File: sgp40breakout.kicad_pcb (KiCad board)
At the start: 2 copper layers, 15 x 11.2 mm, 13 parts, among them J1 Conn_01x04_Male, U1 SGP40, U2 SHT35-DIS

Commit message: add missing file, fix back silk screen
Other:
- board text added: "SGP40 SHT35-DIS VOC Sensor v0.1"
- board text removed: "SGP40 SHT35-D VOC Sensor v0.1"

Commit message: remove most gold plating from mounting hole
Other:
- board text added: "Sensirion SGP40 SHT35-DIS"
- board text added: "v0.1"
- board text removed: "SGP40 SHT35-DIS VOC Sensor v0.1"
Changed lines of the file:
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@@
   (general
     (thickness 1.6002)
-    (drawings 13)
+    (drawings 14)
     (tracks 89)
     (zones 0)
@@
     (mod_text_size 1 1)
     (mod_text_width 0.15)
-    (pad_size 1.524 1.524)
-    (pad_drill 0.762)
+    (pad_size 2.4 2.4)
+    (pad_drill 2.2)
     (pad_to_mask_clearance 0.000051)
     (aux_axis_origin 0 0)
@@
       (effects (font (size 1 1) (thickness 0.15)))
     )
-    (pad 1 thru_hole circle (at 0 0) (size 4.4 4.4) (drill 2.2) (layers *.Cu *.Mask))
+    (pad 1 thru_hole circle (at 0 0) (size 2.4 2.4) (drill 2.2) (layers *.Cu *.Mask))
   )
   (module sgp40breakout:Sensirion_DFN-6-1EP_2.44x2.44mm_P0.8mm (layer F.Cu)
@@
       (net 2 "Net-(C1-Pad2)"))
   )
-  (gr_text "SGP40\nSHT35-DIS\nVOC Sensor\nv0.1" (at 130.302 80.01 270) (layer B.SilkS)
+  (gr_text v0.1 (at 135.636 82.042 270) (layer B.Cu)
+    (effects (font (size 0.8 0.8) (thickness 0.2)) (justify mirror))
+  )
+  (gr_text "Sensirion\nSGP40\nSHT35-DIS" (at 130.302 80.01 270) (layer B.SilkS)
     (effects (font (size 0.8 0.8) (thickness 0.15)) (justify mirror))
   )

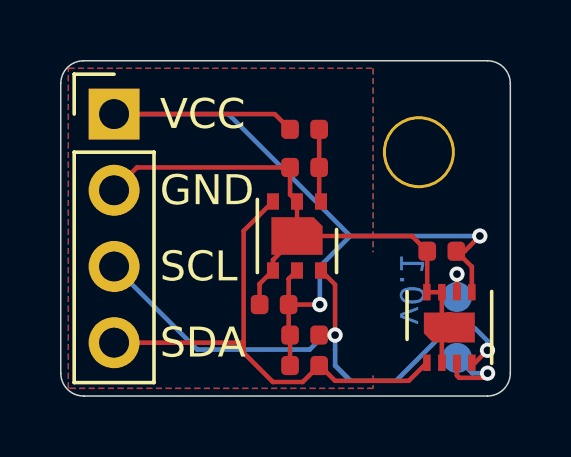
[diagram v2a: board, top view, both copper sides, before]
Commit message: add OSHW logo
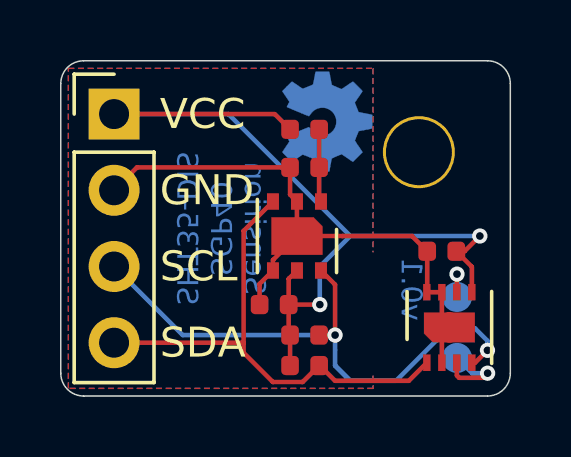
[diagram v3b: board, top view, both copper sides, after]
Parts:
- added REF**: OSHW-Symbol_3.3x3mm_Copper, sgp40breakout:OSHW-Symbol_3.3x3mm_Copper, B.Cu at (132.8, 76.5)

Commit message: assign 3D models and flip mount side of pin header
Using KiCad nightly...
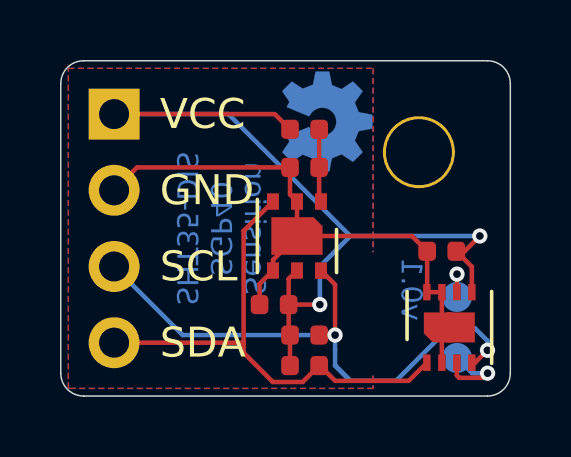
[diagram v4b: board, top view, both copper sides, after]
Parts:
- J1: moved to B.Cu
- turned J1 to 180 degrees
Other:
- net class Default removed

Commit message: revert back to stable KiCad PCB
Convert sgp40breakout.kicad_pcb back to a format readable by the stable
version of KiCad. Move pin header to the back using stable version.
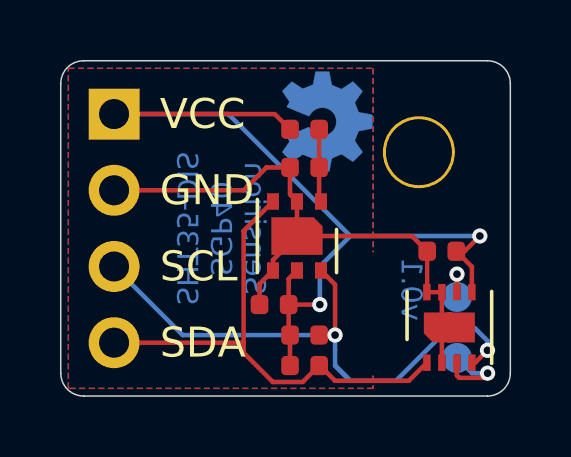
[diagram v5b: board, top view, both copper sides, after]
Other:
- net class Default added: clearance 0.1524, trace_width 0.1524, via_dia 0.508, via_drill 0.254
